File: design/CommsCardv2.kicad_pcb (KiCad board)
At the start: 4 copper layers, 191 parts, among them J1001 USB_B, J201 Conn_01x02, J301 DB9_Male_MountingHoles, J302 DB9_Male_MountingHoles, J303 DB9_Male_MountingHoles, J304 Conn_01x02, J305 Conn_Coaxial, J501 Conn_01x03, J701 Conn_01x03, J901 USB_B, Q301 Q_NMOS_DGS, Q302 Q_NMOS_DGS, U1001 ADUM3160, U201 LT3509EMSE, U301 MAX3387EEUG, U302 MAX3485, U303 TPS28225DRBT, U401 74LV14, U402 74LVC2G00, U403 STWD100xxWY, U404 STWD100xxWY, U405 74AHC157, U501 93C46B, U502 FT4232H, U503 74LV595, U601 74LVC3G14, U602 SN74LV86, U603 501BMILF, U604 74LVC1G80, U605 74LV595, U606 74LV595, U701 93C46B, U702 FT4232H, U703 74LV595, U801 74LVC3G14, U802 SN74LV86, U803 501BMILF, U804 74LVC1G80, U805 74LV595, U806 74LV595, U901 ADUM3160, X501 ASEMB-12MHz, X701 ASEMB-12MHz

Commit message: Duplicating FC1
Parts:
- moved J701 187.2 mm to (199.6, 303.3), turned to 180 degrees
- moved L702 157.9 mm to (93.8, 65.9), turned to 0 degrees
- moved R701 157.3 mm to (97.7, 66.8)
- moved C703 155.9 mm to (93.0, 68.4), turned to 0 degrees
- moved X701 152.8 mm to (93.5, 71.0)
- moved C707 151.0 mm to (95.2, 82.2)
- moved C706 151.0 mm to (95.2, 80.5)
- moved C708 150.9 mm to (95.2, 77.5)
- moved C705 150.0 mm to (90.4, 71.1)
- moved C702 150.0 mm to (97.1, 70.1), turned to 0 degrees
- moved C701 148.9 mm to (80.1, 69.8)
- moved R706 148.9 mm to (80.1, 71.8)
- moved L701 148.9 mm to (79.4, 66.7)
- moved U702 148.8 mm to (88.5, 77.7)
- moved R712 148.7 mm to (102.3, 76.0)
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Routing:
- net /FlightComputer2/EECS: track 0.00 -> 38.9 mm
- net /FlightComputer2/EECLK: track 0.00 -> 38.7 mm
- net /FlightComputer2/EEDATA: track 0.00 -> 38.0 mm, vias 0 -> 2
- net /Watchdog/~FC2_PWREN: track 0.00 -> 36.3 mm, vias 0 -> 2
- net +3V3: track 42.9 -> 78.6 mm, vias 19 -> 36
- net GND: track 53.8 -> 85.2 mm, vias 37 -> 63
- net /FC2_USB/VBUS2: track 0.00 -> 13.2 mm
- net /FlightComputer2/1V8: track 0.00 -> 12.7 mm, vias 0 -> 3
- net Net-(C701-Pad1): track 0.00 -> 12.4 mm
- net /FC2_USB/USB_DM: track 0.00 -> 11.1 mm
- net /FC2_USB/USB_DP: track 0.00 -> 11.1 mm
- net /FC2_USB/USB_PWR: track 0.00 -> 11.0 mm
- net /FC2_USB/USB_GND: track 0.00 -> 10.5 mm, vias 0 -> 7
- net Net-(R710-Pad1): track 0.00 -> 9.98 mm
- net Net-(R711-Pad1): track 0.00 -> 9.50 mm
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
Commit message: Duplicate fills for FC2
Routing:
- added copper zone on PWR2.Cu, net /FlightComputer2/1V8
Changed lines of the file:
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@@
-(kicad_pcb (version 20171130) (host pcbnew "(5.0.0-rc2-dev-30-geb94d2fcd)")
+(kicad_pcb (version 20171130) (host pcbnew "(5.0.0-rc2-dev-41-gce1bd4c6b)")
   (general
     (thickness 1.6)
@@
       )
     )
+  )
+  (zone (net 147) (net_name /FlightComputer2/1V8) (layer PWR2.Cu) (hatch edge 0.508)
+    (priority 4)
+    (connect_pads (clearance 0.127))
+    (min_thickness 0.254)
+    (fill yes (arc_segments 16) (thermal_gap 0.508) (thermal_bridge_width 0.508) (smoothing chamfer) (radius 0.254))
+    (polygon
+      (pts
+        (xy 90.996 75.184) (xy 90.996 73.279) (xy 92.901 73.279) (xy 92.901 82.169) (xy 85.916 82.169)
+        (xy 85.916 80.264) (xy 90.996 80.264)
+      )
+    )
+  )
+  (zone (net 12) (net_name +3V3) (layer PWR2.Cu) (hatch edge 0.508)
+    (priority 1)
+    (connect_pads (clearance 0.127))
+    (min_thickness 0.254)
+    (fill yes (arc_segments 16) (thermal_gap 0.508) (thermal_bridge_width 0.508) (smoothing chamfer) (radius 0.254))
+    (polygon
+      (pts
+        (xy 76.645 38.354) (xy 120.46 38.354) (xy 120.46 84.201) (xy 76.645 84.201)
+      )
+    )

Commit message: Begin layout for high-rate data
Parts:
- moved C803 258.5 mm to (116.6, 95.2), turned to 270 degrees
- moved U802 256.6 mm to (101.3, 95.2)
- moved U806 242.0 mm to (110.2, 95.2)
- moved J701 234.1 mm to (87.8, 97.7)
- moved U805 224.5 mm to (106.3, 122.0)
- moved C804 172.8 mm to (107.2, 86.9), turned to 90 degrees
- moved U804 164.1 mm to (110.1, 86.9), turned to 180 degrees
- moved C806 162.4 mm to (113.2, 90.3), turned to 90 degrees
- moved C801 158.1 mm to (99.1, 108.0), turned to 180 degrees
- moved C805 154.4 mm to (96.7, 111.1)
- moved U801 154.4 mm to (99.1, 105.4)
- moved C807 149.4 mm to (104.5, 113.7)
- moved U803 86.9 mm to (122.9, 95.2)
- moved C802 75.0 mm to (104.3, 90.3), turned to 90 degrees
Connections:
- net Net-(U602-Pad3) renamed /FlightComputer1/LOSComms/RAW_BIPHASE
- net Net-(U603-Pad5) renamed /FlightComputer1/LOSComms/2xCLOCK
- net Net-(U802-Pad3) renamed /FlightComputer2/LOSComms/RAW_BIPHASE
- net Net-(U803-Pad5) renamed /FlightComputer2/LOSComms/2xCLOCK
- C1003 pad 1: /FC2_USB/VBUS2 -> Net-(C1003-Pad1)
- C1004 pad 1: /FC2_USB/VBUS2 -> +5V
- C903 pad 1: /FC1_USB/VBUS2 -> Net-(C903-Pad1)
- C904 pad 1: /FC1_USB/VBUS2 -> +5V
- U1001 pad 12: /FC2_USB/VBUS2 -> Net-(C1003-Pad1)
- U1001 pad 13: /FC2_USB/VBUS2 -> Net-(C1003-Pad1)
- U1001 pad 14: /FC2_USB/VBUS2 -> Net-(C1003-Pad1)
- U1001 pad 16: /FC2_USB/VBUS2 -> +5V
- U503 pad 15: Net-(RN501-Pad8) -> Net-(U503-Pad15)
- U606 pad 4: Net-(U602-Pad9) -> Net-(U602-Pad10)
- U606 pad 5: Net-(U602-Pad10) -> Net-(U602-Pad9)
- U703 pad 15: Net-(RN701-Pad8) -> Net-(U703-Pad15)
- U806 pad 4: Net-(U802-Pad9) -> Net-(U802-Pad10)
- U806 pad 5: Net-(U802-Pad10) -> Net-(U802-Pad9)
- U901 pad 12: /FC1_USB/VBUS2 -> Net-(C903-Pad1)
- U901 pad 13: /FC1_USB/VBUS2 -> Net-(C903-Pad1)
- U901 pad 14: /FC1_USB/VBUS2 -> Net-(C903-Pad1)
- U901 pad 16: /FC1_USB/VBUS2 -> +5V
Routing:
- net Net-(U802-Pad5): track 0.00 -> 6.44 mm
- net GND: track 85.2 -> 88.7 mm, vias 63 -> 66
- net Net-(U802-Pad10): track 0.00 -> 3.39 mm
- net Net-(U802-Pad9): track 0.00 -> 3.39 mm

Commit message: Adjusting LOS
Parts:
- moved U405 75.9 mm to (124.0, 81.8)
- moved U301 58.9 mm to (127.9, 138.8)
- moved U805 19.8 mm to (110.2, 102.7)
- moved C801 7.96 mm to (101.3, 100.3)
- moved U801 3.61 mm to (101.3, 102.6)
- moved C803 1.65 mm to (118.2, 95.2)
- moved C802 1.16 mm to (103.4, 91.1), turned to 180 degrees
- moved C806 1.16 mm to (112.3, 91.1), turned to 180 degrees
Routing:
- net /FlightComputer2/LOSComms/CLK: track 0.00 -> 43.5 mm, vias 0 -> 3
- net /FlightComputer2/LOSComms/DATA: track 0.00 -> 38.4 mm, vias 0 -> 2
- net GND: track 88.7 -> 108.1 mm, vias 66 -> 74
- net /FlightComputer2/LOSComms/DELAY_CLK: track 0.00 -> 18.3 mm
- net /FlightComputer2/LOSComms/RNRZ-L: track 0.00 -> 17.0 mm
- net +3V3: track 78.6 -> 88.9 mm, vias 36 -> 39

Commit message: Layout additional watchdog
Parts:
- moved R403 302.5 mm to (77.5, 54.6), turned to 270 degrees
- moved R406 265.9 mm to (124.0, 51.6), turned to 90 degrees
- moved D401 264.5 mm to (80.0, 49.8), turned to 180 degrees
- moved R405 263.8 mm to (122.2, 51.6), turned to 90 degrees
- moved C401 260.5 mm to (126.8, 60.5), turned to 90 degrees
- moved C404 258.4 mm to (123.7, 69.2), turned to 180 degrees
- moved R402 248.6 mm to (123.7, 73.8)
- moved D403 247.4 mm to (122.9, 43.2)
- moved U401 245.9 mm to (123.8, 65.0)
- moved C403 240.7 mm to (145.2, 70.6), turned to 180 degrees
- moved U404 239.6 mm to (123.7, 71.5)
- moved R404 239.0 mm to (154.7, 53.1), turned to 270 degrees
- moved R407 238.9 mm to (127.9, 77.7)
- moved C405 235.2 mm to (126.4, 103.0), turned to 90 degrees
- moved R401 230.0 mm to (145.2, 75.2)
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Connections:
- U401 pad 3: /Watchdog/~FC2_PWREN -> /FlightComputer1/IN_CHARGE
- U401 pad 4: Net-(R404-Pad2) -> Net-(R405-Pad1)
- U401 pad 5: /FlightComputer1/IN_CHARGE -> Net-(R405-Pad1)
- U401 pad 6: Net-(R405-Pad1) -> Net-(R406-Pad1)
- U401 pad 8: Net-(R406-Pad1) -> Net-(R404-Pad2)
- U401 pad 9: Net-(R405-Pad1) -> /Watchdog/~FC2_PWREN
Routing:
- net Net-(R404-Pad2): track 0.00 -> 40.3 mm
- net Net-(R406-Pad1): track 0.00 -> 15.7 mm
- net Net-(R405-Pad1): track 0.00 -> 14.7 mm
- net Net-(D403-Pad3): track 0.00 -> 9.19 mm
- net Net-(D403-Pad1): track 0.00 -> 7.82 mm
- net +3V3: track 88.9 -> 94.0 mm
- net GND: track 108.1 -> 110.5 mm, vias 74 -> 77
- net /FlightComputer1/IN_CHARGE: track 0.00 -> 1.70 mm
- net /Watchdog/~FC2_PWREN: track 36.3 -> 38.0 mm
- net /Watchdog/~FC1_PWREN: track 36.3 -> 38.0 mm

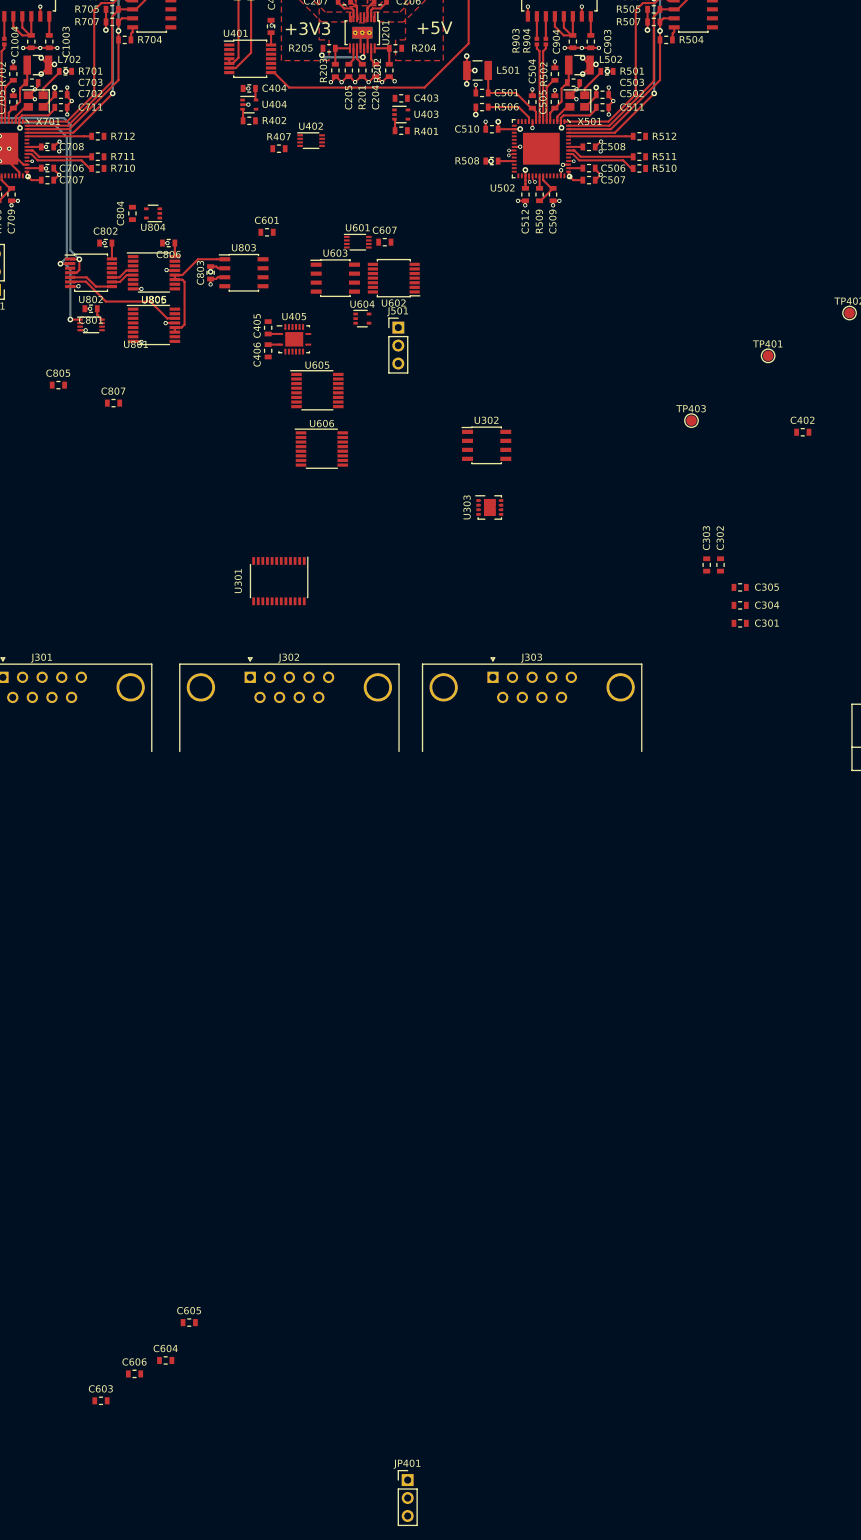
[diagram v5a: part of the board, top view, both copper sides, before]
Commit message: Adding more LOS detail
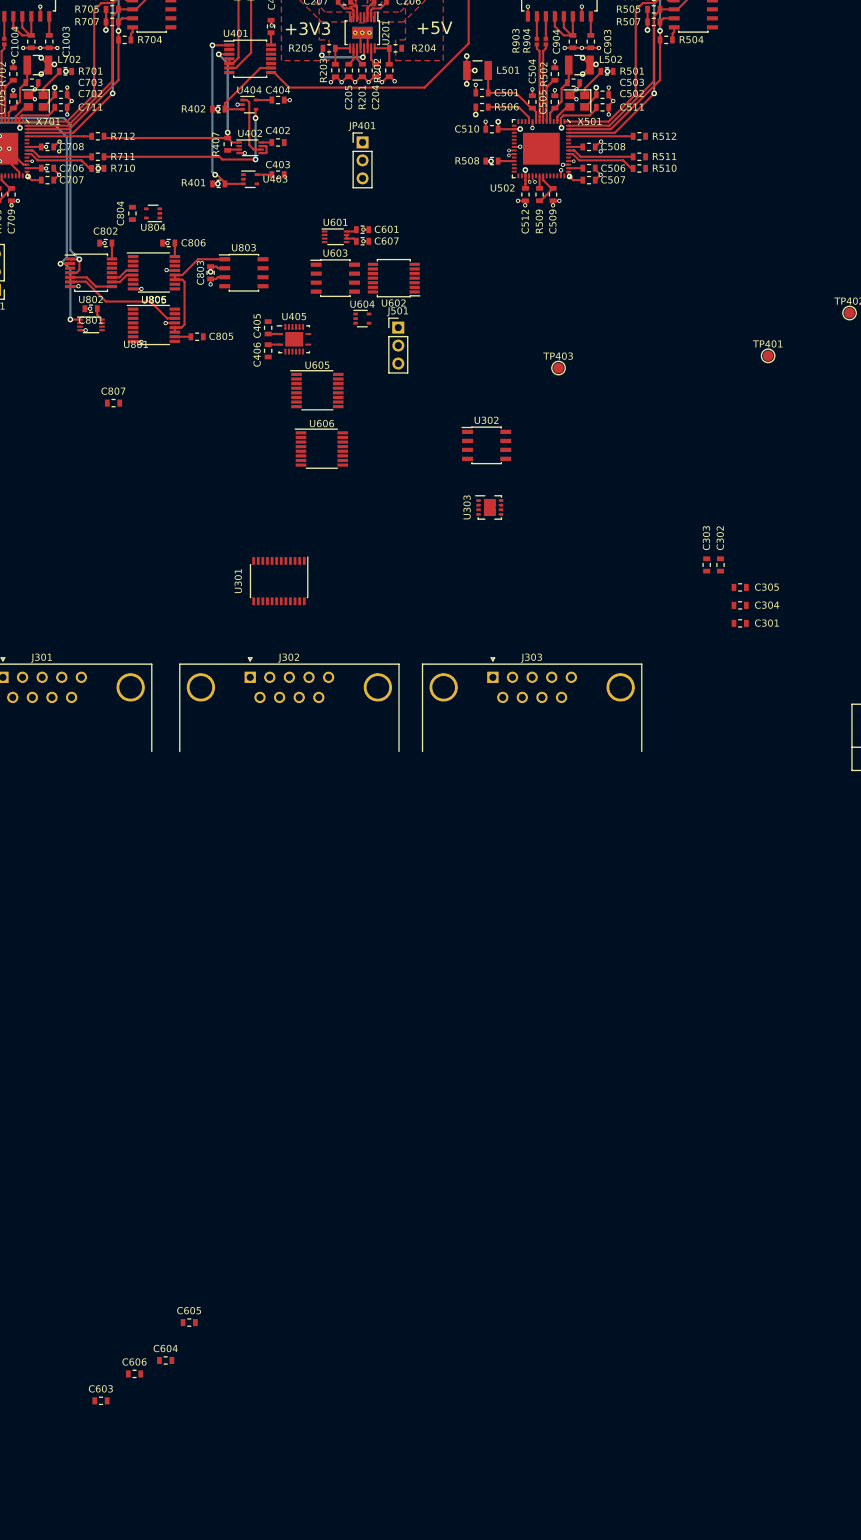
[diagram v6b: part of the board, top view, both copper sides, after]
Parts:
- moved JP401 189.1 mm to (139.7, 76.8)
- moved C402 84.7 mm to (127.8, 76.8)
- moved R401 26.9 mm to (119.4, 82.7), turned to 180 degrees
- moved U403 23.2 mm to (123.8, 82.0)
- moved C805 20.8 mm to (116.3, 104.3)
- moved C403 20.5 mm to (127.8, 81.4), turned to 0 degrees
- moved TP403 20.2 mm to (167.4, 108.7)
- moved C601 13.5 mm to (139.7, 89.2)
- moved U402 8.66 mm to (123.8, 77.6)
- moved R407 7.27 mm to (120.7, 77.1), turned to 90 degrees
- moved R402 4.62 mm to (119.4, 72.1), turned to 180 degrees
- moved C404 4.38 mm to (127.8, 70.9), turned to 0 degrees
- moved U601 3.23 mm to (135.9, 90.2)
- moved C607 3.14 mm to (139.7, 90.8)
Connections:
- C1003 pad 1: Net-(C1003-Pad1) -> +5V
- C1004 pad 1: +5V -> Net-(C1004-Pad1)
- C903 pad 1: Net-(C903-Pad1) -> +5V
- C904 pad 1: +5V -> Net-(C904-Pad1)
- U1001 pad 12: Net-(C1003-Pad1) -> Net-(C1004-Pad1)
- U1001 pad 13: Net-(C1003-Pad1) -> Net-(C1004-Pad1)
- U1001 pad 14: Net-(C1003-Pad1) -> Net-(C1004-Pad1)
- U901 pad 12: Net-(C903-Pad1) -> Net-(C904-Pad1)
- U901 pad 13: Net-(C903-Pad1) -> Net-(C904-Pad1)
- U901 pad 14: Net-(C903-Pad1) -> Net-(C904-Pad1)
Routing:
- net /FlightComputer1/IN_CHARGE: track 1.70 -> 35.0 mm, vias 0 -> 2
- net /Watchdog/FC2_WD: track 0.00 -> 28.7 mm, vias 0 -> 2
- net /Watchdog/~FC1_PWREN: track 38.0 -> 61.8 mm, vias 2 -> 4
- net /FC1_USB/VBUS2: track 13.2 -> 0.00 mm
- net /FC2_USB/VBUS2: track 13.2 -> 0.00 mm
- net Net-(C904-Pad1): track 0.00 -> 10.5 mm
- net Net-(C1004-Pad1): track 0.00 -> 10.5 mm
- net +3V3: track 94.0 -> 104.3 mm, vias 39 -> 42
- net /Watchdog/~FC2_PWREN: track 38.0 -> 48.2 mm
- net /Watchdog/FC2_WDO: track 0.00 -> 9.06 mm
- net +5V: track 0.00 -> 5.37 mm
- net Net-(U402-Pad5): track 0.00 -> 2.44 mm
- net GND: track 110.5 -> 112.7 mm, vias 77 -> 80
- net Net-(C607-Pad1): track 0.00 -> 2.04 mm
- net Net-(R407-Pad1): track 0.00 -> 1.67 mm

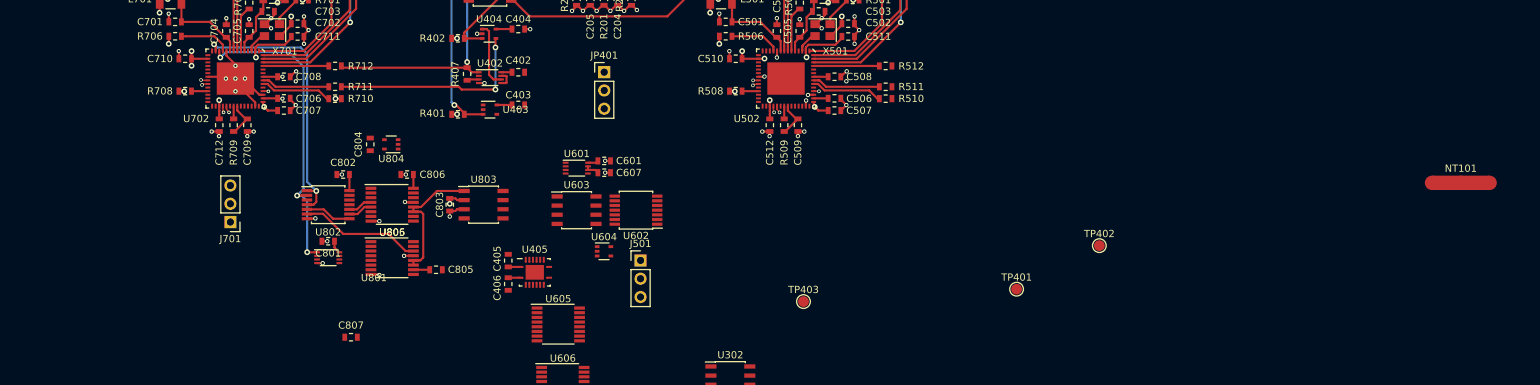
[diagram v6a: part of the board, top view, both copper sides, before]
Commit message: Changing to dual-gate inverters for delay line
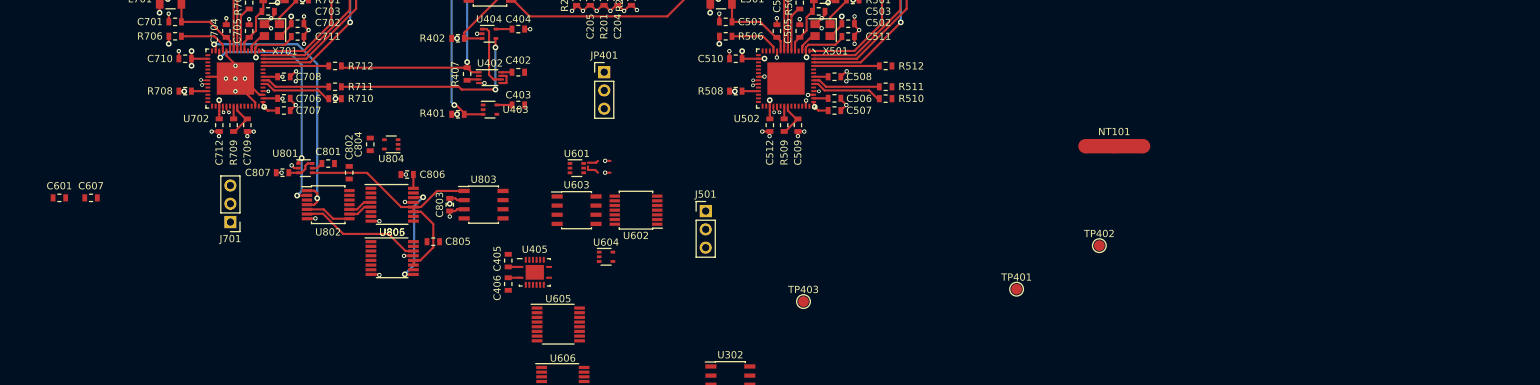
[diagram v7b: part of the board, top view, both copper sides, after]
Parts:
- U601, U801: footprint Package_SO:VSSOP-8_2.3x2mm_P0.5mm -> Package_TO_SOT_SMD:SOT-363_SC-70-6
- moved C601 75.9 mm to (64.0, 94.3)
- moved C607 71.4 mm to (68.4, 94.3)
- moved NT101 48.4 mm to (210.6, 87.1)
- moved C807 24.8 mm to (95.0, 90.8), turned to 180 degrees
- moved U801 12.8 mm to (98.2, 90.2)
- moved J501 11.4 mm to (153.8, 96.1)
- moved C801 10.8 mm to (101.3, 89.5), turned to 0 degrees
- moved C805 3.92 mm to (116.0, 100.4)
- moved C802 0.88 mm to (104.3, 90.8), turned to 90 degrees
- moved U604 0.81 mm to (140.0, 102.5)
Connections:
- U601 pad 2: /FlightComputer1/LOSComms/DELAY_CLK -> GND
- U601 pad 3: Net-(C807-Pad1) -> Net-(C607-Pad1)
- U601 pad 4: GND -> /FlightComputer1/LOSComms/DELAY_CLK
- U601 pad 5: /FlightComputer2/LOSComms/DELAY_CLK -> +3V3
- U801 pad 2: (no net) -> GND
- U801 pad 3: (no net) -> Net-(C807-Pad1)
- U801 pad 4: GND -> /FlightComputer2/LOSComms/DELAY_CLK
- U801 pad 5: (no net) -> +3V3
- U801 pad 6: (no net) -> Net-(C807-Pad1)
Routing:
- net /FlightComputer2/LOSComms/DELAY_CLK: track 18.3 -> 35.5 mm
- net Net-(U805-Pad9): track 0.00 -> 14.3 mm, vias 0 -> 2
- net /FlightComputer2/LOSComms/CLK: track 43.5 -> 34.1 mm
- net +3V3: track 104.3 -> 98.1 mm
- net Net-(C807-Pad1): track 0.00 -> 4.06 mm
- net (no net): track 0.00 -> 3.53 mm
- net Net-(C607-Pad1): track 2.04 -> 0.00 mm
- net /FlightComputer2/LOSComms/DATA: track 38.4 -> 39.5 mm
- net GND: track 112.7 -> 112.3 mm, vias 80 -> 79

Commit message: Finalizing FC1 --- ish
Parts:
- moved C603 115.2 mm to (85.3, 140.7)
- moved C604 115.2 mm to (94.5, 135.0)
- moved C605 115.2 mm to (97.8, 129.6)
- moved C606 115.2 mm to (90.1, 136.9)
- moved C203 111.9 mm to (225.4, 67.8)
- moved C310 111.9 mm to (218.5, 106.5)
- moved C601 75.3 mm to (139.2, 90.2)
- moved J701 41.7 mm to (129.4, 96.3)
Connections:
- U802 pad 1: /FlightComputer2/LOSComms/DATA -> (no net)
- U802 pad 11: (no net) -> /FlightComputer2/LOSComms/RAW_BIPHASE
- U802 pad 12: (no net) -> /FlightComputer2/LOSComms/DATA
- U802 pad 13: (no net) -> /FlightComputer2/LOSComms/CLK
- U802 pad 2: /FlightComputer2/LOSComms/CLK -> (no net)
- U802 pad 3: /FlightComputer2/LOSComms/RAW_BIPHASE -> (no net)
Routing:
- net /FlightComputer2/LOSComms/BIPHASE: track 0.00 -> 22.9 mm
- net /FlightComputer2/LOSComms/2xCLOCK: track 0.00 -> 21.3 mm
- net /FlightComputer2/LOSComms/RNRZ-L: track 17.0 -> 36.1 mm
- net /FlightComputer2/LOSComms/RAW_BIPHASE: track 0.00 -> 11.2 mm
- net +3V3: track 98.1 -> 107.9 mm, vias 42 -> 46
- net GND: track 112.3 -> 119.5 mm, vias 79 -> 80
- net /FlightComputer2/LOSComms/DELAY_CLK: track 35.5 -> 41.2 mm, vias 0 -> 3
- net /FlightComputer2/LOSComms/CLK: track 34.1 -> 38.0 mm, vias 3 -> 2
- net (no net): track 3.53 -> 0.00 mm
- net /FlightComputer2/LOSComms/DATA: track 39.5 -> 42.5 mm
- net Net-(U805-Pad9): track 14.3 -> 13.5 mm
- added copper zone on F.Cu, net GND
